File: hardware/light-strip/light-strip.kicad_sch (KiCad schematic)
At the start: 11 parts, among them J1 Conn_01x01, J2 Conn_01x01

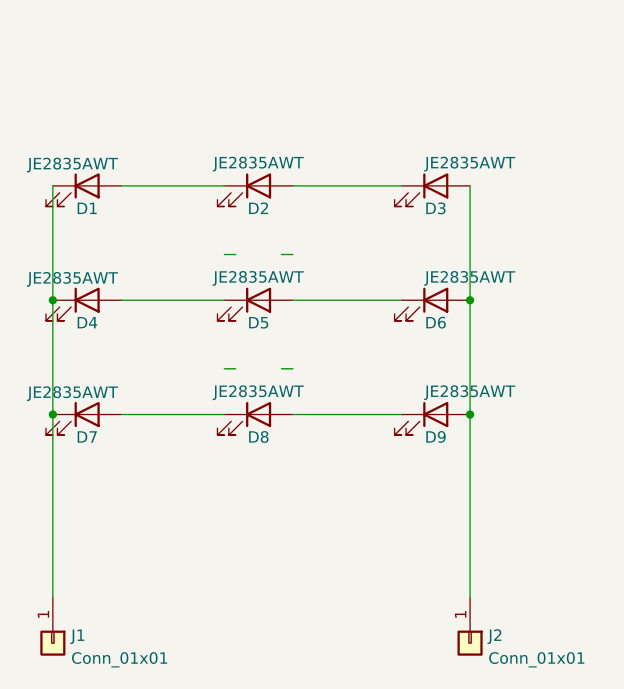
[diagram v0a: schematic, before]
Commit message: Add a second set of pad for symetrical connect Update PCB and ajust size with housing Add 2 mounting holes, just in case Add fabrication files.
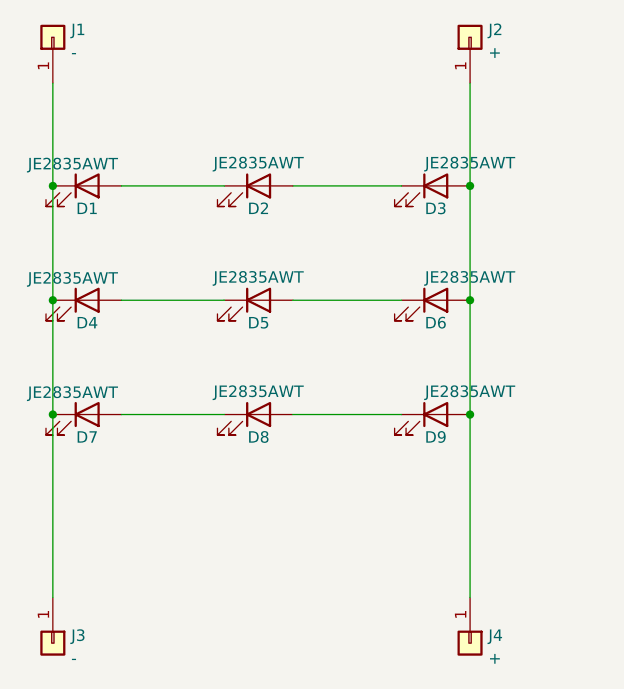
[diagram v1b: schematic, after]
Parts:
- added J1: -, Connector_Wire:SolderWirePad_1x01_SMD_5x10mm, symbol Connector_Generic:Conn_01x01
- added J2: +, Connector_Wire:SolderWirePad_1x01_SMD_5x10mm, symbol Connector_Generic:Conn_01x01
- J3: renamed from J1; value Conn_01x01 -> -
- J4: renamed from J2; value Conn_01x01 -> +
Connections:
- net at D3.2 (A), D6.2 (A), D9.2 (A)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: now also J2.1 (Pin_1)
- net at D1.1 (K), D4.1 (K), D7.1 (K)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: now also J1.1 (Pin_1)
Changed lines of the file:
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@@
   (junction (at 169.545 59.69) (diameter 0) (color 0 0 0 0)
   )
+  (junction (at 169.545 46.99) (diameter 0) (color 0 0 0 0)
+  )
   (junction (at 123.19 59.69) (diameter 0) (color 0 0 0 0)
   )
@@
   (junction (at 123.19 72.39) (diameter 0) (color 0 0 0 0)
   )
+  (junction (at 123.19 46.99) (diameter 0) (color 0 0 0 0)
+  )
   (wire (pts (xy 130.81 46.99) (xy 142.24 46.99))
     (stroke (width 0) (type default) (color 0 0 0 0))
@@
     (stroke (width 0) (type default) (color 0 0 0 0))
   )
-  (wire (pts (xy 143.51 67.31) (xy 142.24 67.31))
-    (stroke (width 0) (type default) (color 0 0 0 0))
-  )
   (wire (pts (xy 123.19 92.71) (xy 123.19 72.39))
     (stroke (width 0) (type default) (color 0 0 0 0))
   )
-  (wire (pts (xy 148.59 54.61) (xy 149.86 54.61))
-    (stroke (width 0) (type default) (color 0 0 0 0))
-  )
   (wire (pts (xy 149.86 59.69) (xy 161.925 59.69))
     (stroke (width 0) (type default) (color 0 0 0 0))
   )
-  (wire (pts (xy 143.51 54.61) (xy 142.24 54.61))
-    (stroke (width 0) (type default) (color 0 0 0 0))
-  )
   (wire (pts (xy 169.545 59.69) (xy 169.545 72.39))
     (stroke (width 0) (type default) (color 0 0 0 0))
@@
     (stroke (width 0) (type default) (color 0 0 0 0))
   )
+  (wire (pts (xy 169.545 35.56) (xy 169.545 46.99))
+    (stroke (width 0) (type default) (color 0 0 0 0))
+  )
   (wire (pts (xy 149.86 72.39) (xy 161.925 72.39))
     (stroke (width 0) (type default) (color 0 0 0 0))
@@
     (stroke (width 0) (type default) (color 0 0 0 0))
   )
-  (wire (pts (xy 148.59 67.31) (xy 149.86 67.31))
-    (stroke (width 0) (type default) (color 0 0 0 0))
-  )
   (wire (pts (xy 123.19 59.69) (xy 123.19 72.39))
     (stroke (width 0) (type default) (color 0 0 0 0))
   )
+  (wire (pts (xy 123.19 35.56) (xy 123.19 46.99))
+    (stroke (width 0) (type default) (color 0 0 0 0))
+  )
   (wire (pts (xy 123.19 46.99) (xy 123.19 59.69))
     (stroke (width 0) (type default) (color 0 0 0 0))
+  )
+  (symbol (lib_id "Connector_Generic:Conn_01x01") (at 169.545 30.48 90) (unit 1)
+    (in_bom yes) (on_board yes) (fields_autoplaced)
+    (property "Reference" "J2" (id 0) (at 171.577 29.6453 90)
+      (effects (font (size 1.27 1.27)) (justify right))
+    )
+    (property "Value" "+" (id 1) (at 171.577 32.1822 90)
+      (effects (font (size 1.27 1.27)) (justify right))
+    )
+    (property "Footprint" "Connector_Wire:SolderWirePad_1x01_SMD_5x10mm" (id 2) (at 169.545 30.48 0)
+      (effects (font (size 1.27 1.27)) hide)
+    )
+    (property "Datasheet" "~" (id 3) (at 169.545 30.48 0)
+      (effects (font (size 1.27 1.27)) hide)
+    )
+    (pin "1")
   )
   (symbol (lib_id "Device:LED") (at 146.05 46.99 0) (unit 1)
@@
   (symbol (lib_id "Connector_Generic:Conn_01x01") (at 169.545 97.79 270) (unit 1)
     (in_bom yes) (on_board yes) (fields_autoplaced)
-    (property "Reference" "J2" (id 0) (at 171.577 96.9553 90)
+    (property "Reference" "J4" (id 0) (at 171.577 96.9553 90)
       (effects (font (size 1.27 1.27)) (justify left))
     )
-    (property "Value" "Conn_01x01" (id 1) (at 171.577 99.4922 90)
+    (property "Value" "+" (id 1) (at 171.577 99.4922 90)
       (effects (font (size 1.27 1.27)) (justify left))
     )
@@
     (pin "2")
   )
+  (symbol (lib_id "Connector_Generic:Conn_01x01") (at 123.19 30.48 90) (unit 1)
+    (in_bom yes) (on_board yes) (fields_autoplaced)
+    (property "Reference" "J1" (id 0) (at 125.222 29.6453 90)
+      (effects (font (size 1.27 1.27)) (justify right))
+    )
+    (property "Value" "-" (id 1) (at 125.222 32.1822 90)
+      (effects (font (size 1.27 1.27)) (justify right))
+    )
+    (property "Footprint" "Connector_Wire:SolderWirePad_1x01_SMD_5x10mm" (id 2) (at 123.19 30.48 0)
+      (effects (font (size 1.27 1.27)) hide)
+    )
+    (property "Datasheet" "~" (id 3) (at 123.19 30.48 0)
+      (effects (font (size 1.27 1.27)) hide)
+    )
+    (pin "1")
+  )
   (symbol (lib_id "Device:LED") (at 127 72.39 0) (unit 1)
     (in_bom yes) (on_board yes)
@@
   (symbol (lib_id "Connector_Generic:Conn_01x01") (at 123.19 97.79 270) (unit 1)
     (in_bom yes) (on_board yes) (fields_autoplaced)
-    (property "Reference" "J1" (id 0) (at 125.222 96.9553 90)
+    (property "Reference" "J3" (id 0) (at 125.222 96.9553 90)
       (effects (font (size 1.27 1.27)) (justify left))
     )
-    (property "Value" "Conn_01x01" (id 1) (at 125.222 99.4922 90)
+    (property "Value" "-" (id 1) (at 125.222 99.4922 90)
       (effects (font (size 1.27 1.27)) (justify left))
     )
@@
       (reference "D9") (unit 1) (value "JE2835AWT") (footprint "LED_SMD:LED_PLCC_2835_Handsoldering")
     )
+    (path "/71ccfbed-7612-4fca-9581-f8fe9fdcdb5c"
+      (reference "J1") (unit 1) (value "-") (footprint "Connector_Wire:SolderWirePad_1x01_SMD_5x10mm")
+    )
+    (path "/01422004-0ff9-44a2-a82b-37250beb647e"
+      (reference "J2") (unit 1) (value "+") (footprint "Connector_Wire:SolderWirePad_1x01_SMD_5x10mm")
+    )
     (path "/f881b220-3e78-410e-86e1-497d7484ab1f"
-      (reference "J1") (unit 1) (value "Conn_01x01") (footprint "Connector_Wire:SolderWirePad_1x01_SMD_5x10mm")
+      (reference "J3") (unit 1) (value "-") (footprint "Connector_Wire:SolderWirePad_1x01_SMD_5x10mm")
     )
     (path "/2e9263bc-cb47-4159-a3be-0606a3388532"
-      (reference "J2") (unit 1) (value "Conn_01x01") (footprint "Connector_Wire:SolderWirePad_1x01_SMD_5x10mm")
-    )
-  )
+      (reference "J4") (unit 1) (value "+") (footprint "Connector_Wire:SolderWirePad_1x01_SMD_5x10mm")
+    )
+  )
